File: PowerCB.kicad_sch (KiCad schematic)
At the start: 16 parts, among them J2 Mounting_1, J3 Mounting_2, J6 Conn_01x02_Male, J7 Conn_01x02_Male, J8 Conn_01x02_Male, J9 Conn_01x02_Male, U1 TPS73633DBV, U2 USB-C-Power

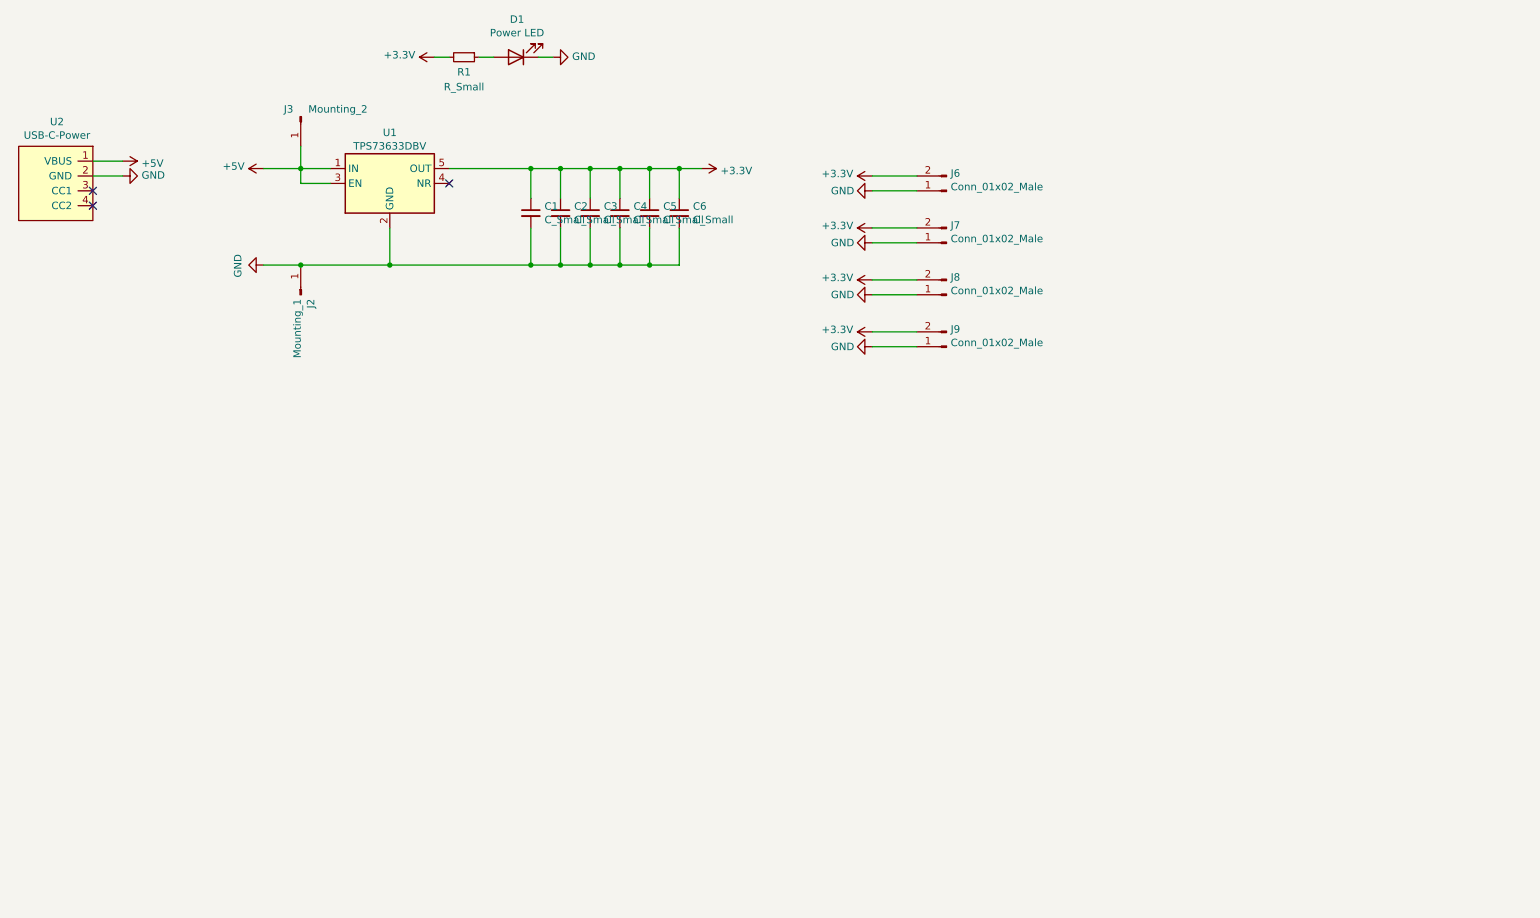
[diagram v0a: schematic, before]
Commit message: feat: M3 instead of M2 mounting holes
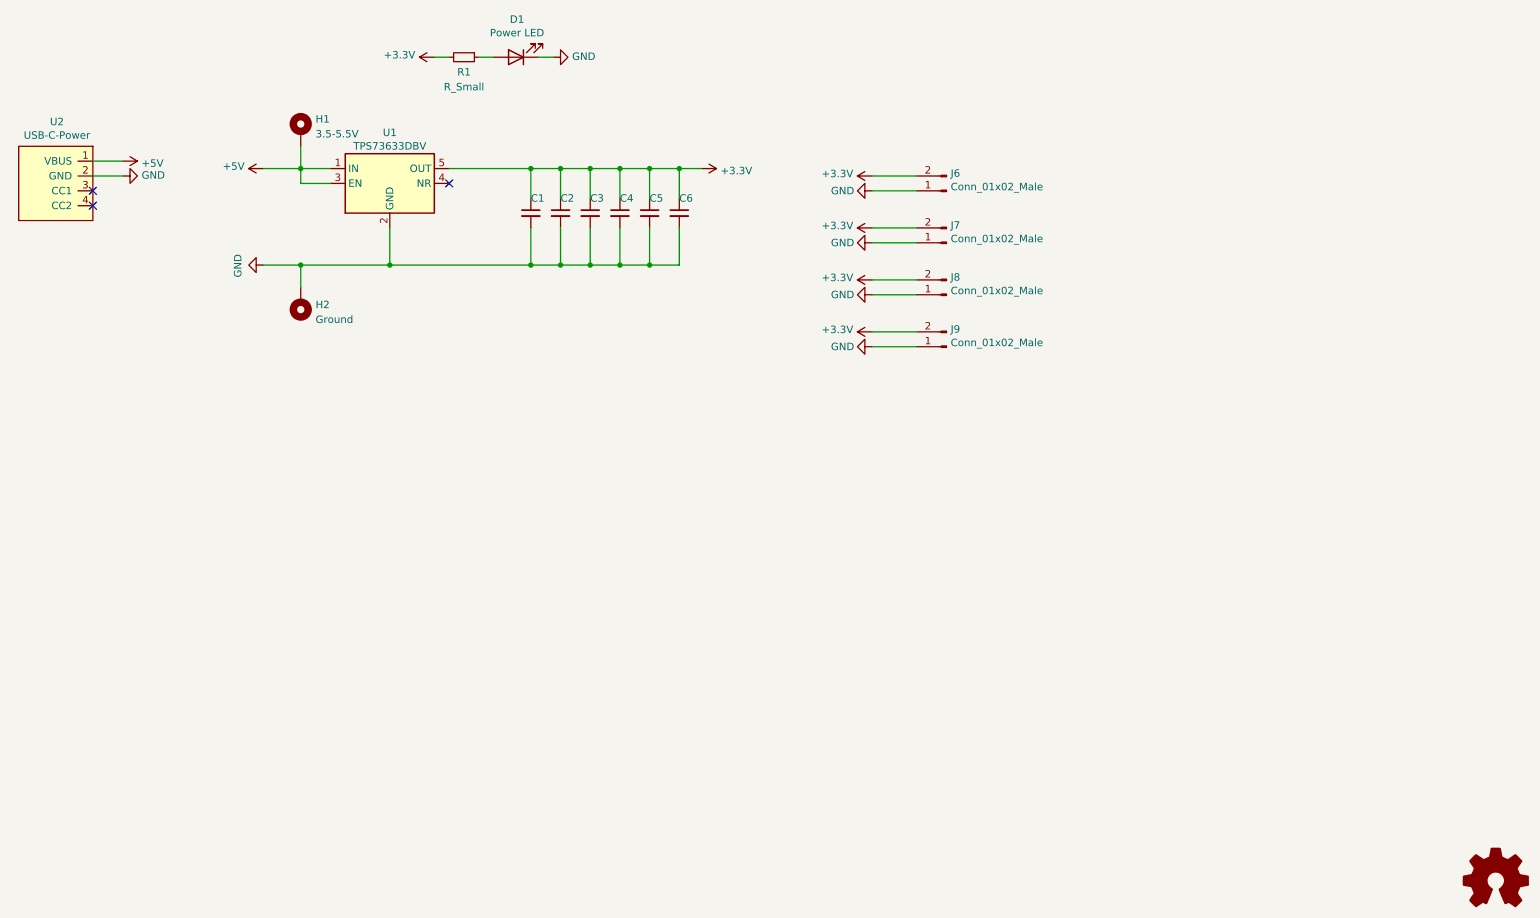
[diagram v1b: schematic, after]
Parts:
- removed J2: Mounting_1, MountingHole:MountingHole_2.2mm_M2_DIN965_Pad, symbol Connector:Conn_01x01_Male
- removed J3: Mounting_2, MountingHole:MountingHole_2.2mm_M2_DIN965_Pad, symbol Connector:Conn_01x01_Male
- added H1: 3.5-5.5V, MountingHole:MountingHole_3.2mm_M3_DIN965_Pad, symbol Mechanical:MountingHole_Pad
- added H2: Ground, MountingHole:MountingHole_3.2mm_M3_DIN965_Pad, symbol Mechanical:MountingHole_Pad
- U2: footprint (none) -> USB-C:UJC-HP-3-SMT-TR
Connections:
- net +5V: now also H1.1
- net GND: now also H2.1

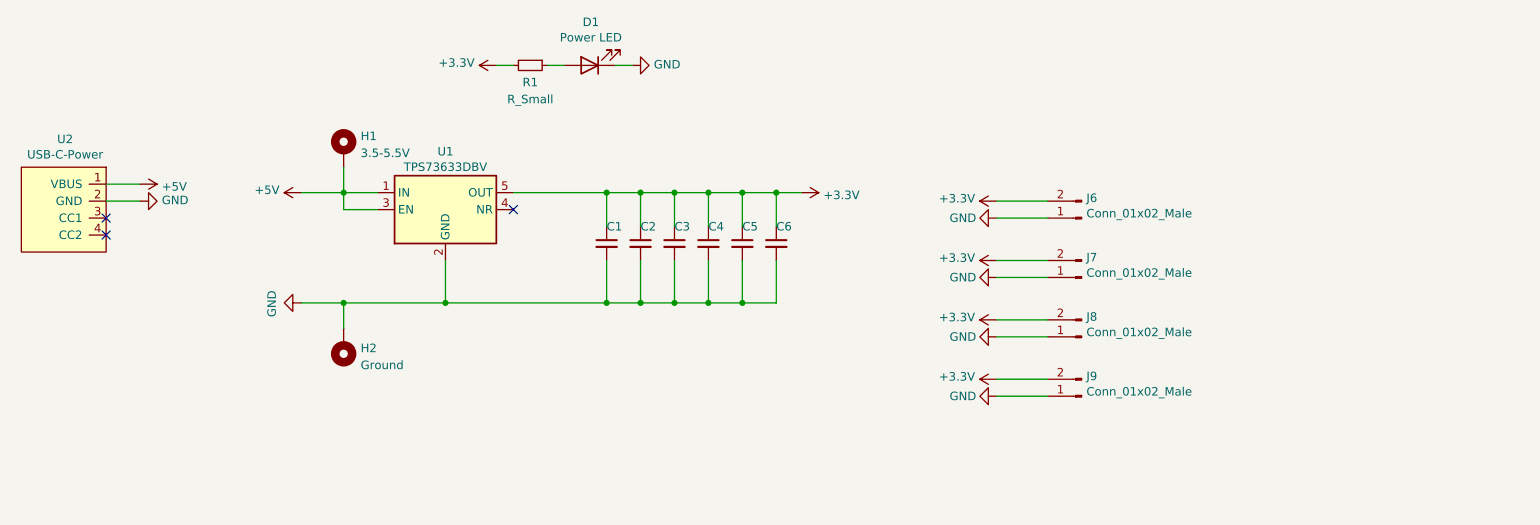
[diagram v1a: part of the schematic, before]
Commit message: fix: missing USB-C CC pulldown resistors
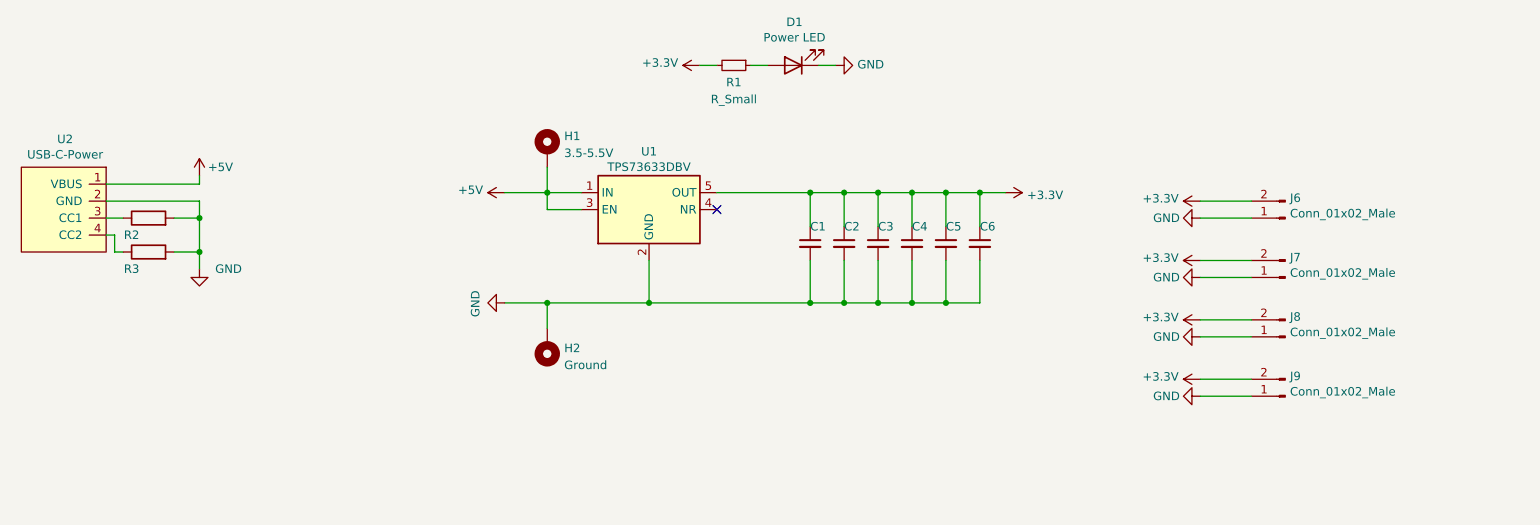
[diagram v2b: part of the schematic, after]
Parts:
- added R2, R3: (no value), symbol Device:R
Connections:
- net GND: now also R2.2, R3.2
- net at U2.3 (CC1): now also R2.1
- net at U2.4 (CC2): now also R3.1
- no-connect marks 3 -> 1
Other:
- moved on the sheet: C1, C2, C3, C4, C5, C6, D1, H1, H2, J6, J7, J8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
